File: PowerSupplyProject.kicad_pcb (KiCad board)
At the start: 2 copper layers, 0 parts

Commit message: create pcb design, route and copper fills
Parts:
- added C1: 10u, Capacitor_THT:C_Disc_D3.0mm_W1.6mm_P2.50mm, F.Cu at (126.7, 77.5)
- added C2: 0.1u, Capacitor_THT:C_Disc_D3.0mm_W1.6mm_P2.50mm, F.Cu at (119.4, 77.5)
- added C3: 1u, Capacitor_THT:C_Disc_D3.0mm_W1.6mm_P2.50mm, F.Cu at (120.9, 111.0)
- added D1: LED, LED_THT:LED_D5.0mm, F.Cu at (136.9, 94.5)
- added J1: Conn_01x02_Pin, Connector_PinHeader_2.54mm:PinHeader_1x02_P2.54mm_Vertical, F.Cu at (144.3, 70.1)
- added J2: Conn_01x02_Pin, Connector_PinHeader_2.54mm:PinHeader_1x02_P2.54mm_Vertical, F.Cu at (144.3, 115.9)
- added J3: Conn_01x03_Pin, Connector_PinHeader_2.54mm:PinHeader_1x03_P2.54mm_Vertical, F.Cu at (125.2, 71.1)
- added J4: Conn_01x03_Pin, Connector_PinHeader_2.54mm:PinHeader_1x03_P2.54mm_Vertical, F.Cu at (126.0, 117.6)
- added J5: Screw_Terminal_01x02, TerminalBlockUpdate:TerminalBlock_bornier-2_P5.08mm, F.Cu at (133.0, 72.3)
- added J7: Screw_Terminal_01x02, TerminalBlockUpdate:TerminalBlock_bornier-2_P5.08mm, F.Cu at (133.0, 116.2)
- added J8: Barrel_Jack_Switch, Connector_BarrelJack:BarrelJack_Horizontal, F.Cu at (130.7, 93.2)
- added R1: 330, Resistor_THT:R_Axial_DIN0204_L3.6mm_D1.6mm_P7.62mm_Horizontal, F.Cu at (133.1, 101.9)
- added R2: 330, Resistor_THT:R_Axial_DIN0204_L3.6mm_D1.6mm_P7.62mm_Horizontal, F.Cu at (127.5, 113.8)
- added R3: 560, Resistor_THT:R_Axial_DIN0204_L3.6mm_D1.6mm_P7.62mm_Horizontal, F.Cu at (130.6, 109.5)
- added SW1: EG1218, EG1218:EG1218, F.Cu at (132.2, 79.8)
- added U1: LM7805_TO220, Package_TO_SOT_THT:TO-220-3_Vertical, F.Cu at (124.7, 84.1)
- added U2: LM317_TO-220, Package_TO_SOT_THT:TO-220-3_Vertical, F.Cu at (125.2, 103.1)
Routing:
- net /PWR_output: track 0.00 -> 92.0 mm
- net /3.3V: track 0.00 -> 61.2 mm
- net /5V: track 0.00 -> 49.3 mm
- net /12V: track 0.00 -> 49.0 mm
- net Net-(D1-A): track 0.00 -> 28.3 mm
- net /3V: track 0.00 -> 19.1 mm
- net /PWR_input: track 0.00 -> 14.1 mm
- net Net-(U2-ADJ): track 0.00 -> 8.40 mm
- net Net-(U1-VO): track 0.00 -> 6.69 mm
- added copper zone on B.Cu, net GND
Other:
- board outline added: 30.2 x 52.3 mm

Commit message: fix route
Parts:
- R1: value 330 -> 330R
- R3: value 560 -> 560R
- U1: value LM7805_TO220 -> LM7805
- U2: value LM317_TO-220 -> LM317
- moved R2 22.9 mm to (134.9, 92.1), turned to 90 degrees
- moved D1 3.52 mm to (136.0, 97.9)
- moved U1 3.11 mm to (122.0, 85.6), turned to 0 degrees
- moved R1 2.02 mm to (134.9, 102.8)
- moved U2 1.88 mm to (127.1, 103.1)
- moved R3 1.44 mm to (131.5, 110.5)
- moved C3 1.12 mm to (120.9, 109.9)
- moved J4 0.76 mm to (125.2, 117.6)
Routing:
- net Net-(D1-A): track 28.3 -> 3.69 mm
- net /12V: track 49.0 -> 60.0 mm
- net Net-(U1-VO): track 6.69 -> 13.6 mm
- net /3.3V: track 61.2 -> 63.1 mm
- net /3V: track 19.1 -> 20.4 mm
- net /PWR_output: track 92.0 -> 93.1 mm
- net Net-(U2-ADJ): track 8.40 -> 9.17 mm

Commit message: adding silkscreen
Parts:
- R2: value 330 -> 330R
- moved C3 1.16 mm to (120.6, 111.0)
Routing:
- net /3V: track 20.4 -> 21.6 mm
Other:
- board text added: "+"
- board text added: "-"
- board text added: "3.3V"
- board text added: "5V"
- board text added: "GND"
- board text added: "OFF"
- board text added: "ON"
- board text added: "V1.0 Power Supply"
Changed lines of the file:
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@@
 			(at -7.8796 -3.6576 0)
 			(layer "F.Fab")
+			(hide yes)
 			(effects
 				(font
@@
 		(tags "EG1218 ")
 		(property "Reference" "SW1"
-			(at -2.9972 5.1524 0)
+			(at 2.794 6.016 0)
 			(unlocked yes)
 			(layer "F.SilkS")
@@
 			(unlocked yes)
 			(layer "F.Fab")
+			(hide yes)
 			(effects
 				(font
@@
 		)
 		(fp_text user "*"
-			(at -2.5019 0 90)
-			(layer "F.SilkS")
+			(at -1.4224 -0.0292 90)
+			(unlocked yes)
+			(layer "F.Fab")
 			(effects
 				(font
@@
 		)
 		(fp_text user "*"
-			(at -2.5019 0 90)
-			(unlocked yes)
-			(layer "F.SilkS")
+			(at -1.6129 0 90)
+			(layer "F.Fab")
 			(effects
 				(font
@@
 		)
 		(fp_text user "*"
-			(at -1.6129 0 90)
-			(unlocked yes)
+			(at -1.4732 2.3584 90)
 			(layer "F.Fab")
 			(effects
@@
 		)
 		(fp_text user "*"
-			(at -1.6129 0 90)
+			(at -1.4224 5.8636 90)
+			(unlocked yes)
 			(layer "F.Fab")
 			(effects
@@
 		)
 		(fp_text user "${REFERENCE}"
-			(at -1.524 2.714 0)
+			(at 0.3048 6.524 0)
 			(unlocked yes)
 			(layer "F.Fab")
@@
 			(at 2.54 5.08 0)
 			(layer "F.Fab")
+			(hide yes)
 			(effects
 				(font
@@
 		(tags "Through hole pin header THT 1x02 2.54mm single row")
 		(property "Reference" "J1"
-			(at -2.5908 1.27 90)
+			(at -2.6924 3.5052 90)
 			(layer "F.SilkS")
 			(effects
@@
 			(at 0 4.92 0)
 			(layer "B.Fab")
+			(hide yes)
 			(effects
 				(font
@@
 		(tags "terminal block bornier2")
 		(property "Reference" "J5"
-			(at -3.6931 2.088 90)
+			(at -3.4391 3.5104 90)
 			(layer "F.SilkS")
 			(effects
@@
 			(at 2.54 5.08 0)
 			(layer "F.Fab")
+			(hide yes)
 			(effects
 				(font
@@
 		(tags "TO-220-3 Vertical RM 2.54mm")
 		(property "Reference" "U2"
-			(at 0.5588 -4.1656 0)
+			(at 0 -4.3688 0)
 			(layer "F.SilkS")
 			(effects
@@
 		)
 		(property "Value" "LM317"
-			(at 2.54 2.2 0)
+			(at 3.6576 -4.3688 0)
 			(layer "F.SilkS")
 			(effects
@@
 	(footprint "Capacitor_THT:C_Disc_D3.0mm_W1.6mm_P2.50mm"
 		(layer "F.Cu")
-		(at 120.8932 109.8804)
+		(at 120.5684 110.998)
 		(descr "C, Disc series, Radial, pin pitch=2.50mm, diameter*width=3.0*1.6mm^2, Capacitor, http://www.vishay.com/docs/45233/krseries.pdf")
 		(tags "C Disc series Radial pin pitch 2.50mm diameter 3.0mm width 1.6mm Capacitor")
@@
 			)
 		)
-		(property "Value" "330"
+		(property "Value" "330R"
 			(at 6.4516 1.8288 90)
 			(layer "F.SilkS")
@@
 		(tags "Through hole pin header THT 1x03 2.54mm single row")
 		(property "Reference" "J3"
-			(at 2.54 -0.8128 180)
+			(at -1.1176 -2.54 0)
 			(layer "F.SilkS")
 			(effects
@@
 			(at 0 7.46 90)
 			(layer "F.Fab")
+			(hide yes)
 			(effects
 				(font
@@
 		(tags "Through hole pin header THT 1x03 2.54mm single row")
 		(property "Reference" "J4"
-			(at -2.6924 -0.6604 180)
+			(at 1.1176 -2.794 180)
 			(layer "F.SilkS")
 			(effects
@@
 			(at 0 7.46 90)
 			(layer "F.Fab")
+			(hide yes)
 			(effects
 				(font
@@
 		(tags "Through hole pin header THT 1x02 2.54mm single row")
 		(property "Reference" "J2"
-			(at -2.8448 0.1524 90)
+			(at -2.6924 2.5908 90)
 			(layer "F.SilkS")
 			(effects
@@
 			(at 0 4.92 0)
 			(layer "F.Fab")
+			(hide yes)
 			(effects
 				(font
@@
 		(layer "Edge.Cuts")
 	)
+	(gr_text "5V"
+		(at 118.9736 115.7732 0)
+		(layer "F.SilkS")
+		(effects
+			(font
+				(size 1 1)
+				(thickness 0.2)
+				(bold yes)
+			)
+			(justify left bottom)
+		)
+	)
+	(gr_text "5V"
+		(at 119.0244 74.168 0)
+		(layer "F.SilkS")
+		(effects
+			(font
+				(size 1 1)
+				(thickness 0.2)
+				(bold yes)
+			)
+			(justify left bottom)
+		)
+	)
+	(gr_text "3.3V"
+		(at 123.952 74.2188 0)
+		(layer "F.SilkS")
+		(effects
+			(font
+				(size 1 1)
+				(thickness 0.2)
+				(bold yes)
+			)
+			(justify left bottom)
+		)
+	)
+	(gr_text "3.3V"
+		(at 124.1044 115.7732 0)
+		(layer "F.SilkS")
+		(effects
+			(font
+				(size 1 1)
+				(thickness 0.2)
+				(bold yes)
+			)
+			(justify left bottom)
+		)
+	)
+	(gr_text "ON"
+		(at 131.0132 83.5152 0)
+		(layer "F.SilkS")
+		(effects
+			(font
+				(size 1 1)
+				(thickness 0.2)
+				(bold yes)
+			)
+			(justify left bottom)
+		)
+	)
+	(gr_text "OFF"
+		(at 135.9916 83.566 0)
+		(layer "F.SilkS")
+		(effects
+			(font
+				(size 1 1)
+				(thickness 0.2)
+				(bold yes)
+			)
+			(justify left bottom)
+		)
+	)
+	(gr_text "-"
+		(at 136.8552 98.1964 0)
+		(layer "F.SilkS")
+		(effects
+			(font
+				(size 1 1)
+				(thickness 0.2)
+				(bold yes)
+			)
+			(justify left bottom)
+		)
+	)
+	(gr_text "+"
+		(at 136.9568 96.1644 0)
+		(layer "F.SilkS")
+		(effects
+			(font
+				(size 1 1)
+				(thickness 0.2)
+				(bold yes)
+			)
+			(justify left bottom)
+		)
+	)
+	(gr_text "GND"
+		(at 130.048 118.0592 90)
+		(layer "F.SilkS")
+		(effects
+			(font
+				(size 1 1)
+				(thickness 0.2)
+				(bold yes)
+			)
+			(justify left bottom)
+		)
+	)
+	(gr_text "GND"
+		(at 130.0988 73.9648 90)
+		(layer "F.SilkS")
+		(effects
+			(font
+				(size 1 1)
+				(thickness 0.2)
+				(bold yes)
+			)
+			(justify left bottom)
+		)
+	)
+	(gr_text "GND"
+		(at 142.1892 71.8312 90)
+		(layer "F.SilkS")
+		(effects
+			(font
+				(size 1 1)
+				(thickness 0.2)
+				(bold yes)
+			)
+			(justify left bottom)
+		)
+	)
+	(gr_text "GND"
+		(at 142.1892 117.0432 90)
+		(layer "F.SilkS")
+		(effects
+			(font
+				(size 1 1)
+				(thickness 0.2)
+				(bold yes)
+			)
+			(justify left bottom)
+		)
+	)
+	(gr_text "V1.0\nPower\nSupply"
+		(at 122.0724 92.3544 90)
+		(layer "B.SilkS")
+		(effects
+			(font
+				(size 1 1)
+				(thickness 0.1)
+			)
+			(justify left bottom mirror)
+		)
+	)
 	(segment
 		(start 132.16 79.756)
@@
 	)
 	(segment
-		(start 120.8932 106.7924)
-		(end 124.5616 103.124)
+		(start 124.5616 103.124)
+		(end 120.5684 107.1172)
 		(width 0.25)
 		(layer "F.Cu")
@@
 	)
 	(segment
-		(start 120.8932 109.8804)
-		(end 120.8932 106.7924)
+		(start 120.5684 107.1172)
+		(end 120.5684 110.998)
 		(width 0.25)
 		(layer "F.Cu")

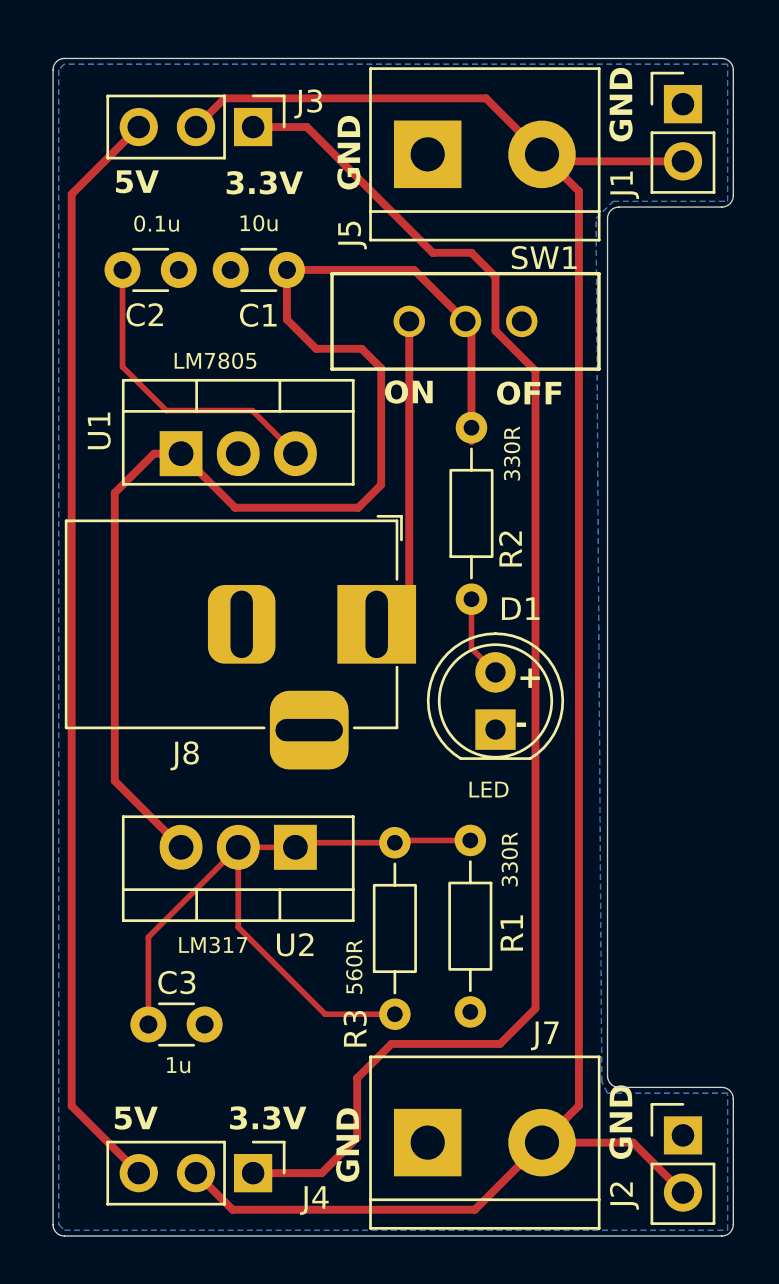
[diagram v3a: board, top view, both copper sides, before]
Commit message: resetting the grid for DfM purposes
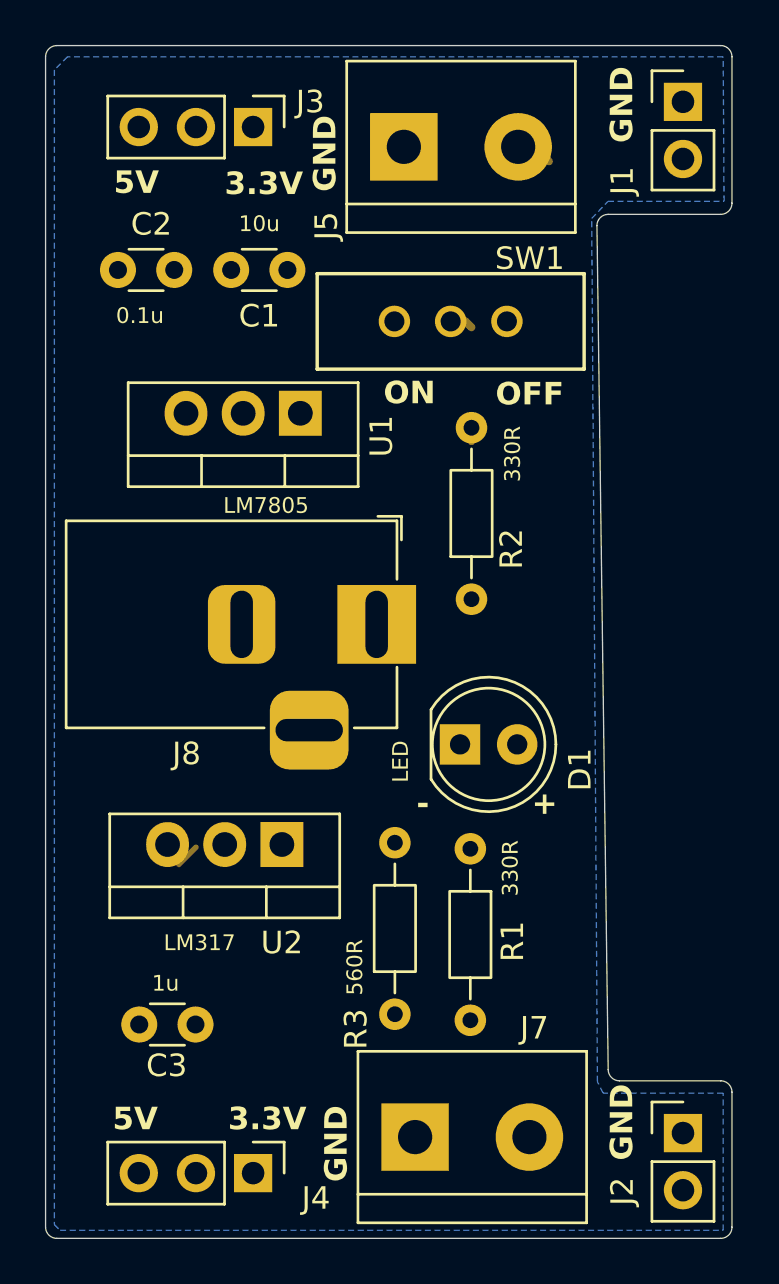
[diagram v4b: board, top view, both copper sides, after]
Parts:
- moved U1 5.59 mm to (127.3, 83.8), turned to 180 degrees
- moved C2 2.30 mm to (121.7, 77.5), turned to 180 degrees
- moved C3 2.09 mm to (122.7, 111.0), turned to 180 degrees
- moved D1 1.71 mm to (134.4, 98.6), turned to 0 degrees
- moved J5 1.11 mm to (131.9, 72.0)
- moved SW1 0.66 mm to (131.5, 79.8)
- moved U2 0.61 mm to (126.5, 103.0)
- moved J7 0.61 mm to (132.4, 116.0)
- moved R1 0.37 mm to (134.9, 103.2)
- moved J1 0.10 mm to (144.3, 70.0)
- moved J2 0.10 mm to (144.3, 115.8)
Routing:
- net /PWR_output: track 93.1 -> 0.44 mm
- net /3.3V: track 63.1 -> 0.00 mm
- net /12V: track 60.0 -> 2.99 mm
- net /5V: track 49.0 -> 0.00 mm
- net /3V: track 21.6 -> 0.00 mm
- net Net-(U1-VO): track 13.6 -> 0.00 mm
- net /PWR_input: track 14.1 -> 2.04 mm
- net Net-(U2-ADJ): track 9.17 -> 0.43 mm
- net Net-(D1-A): track 3.69 -> 0.00 mm
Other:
- board size 30.2 x 52.3 mm -> 30.5 x 53 mm

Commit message: Align all component
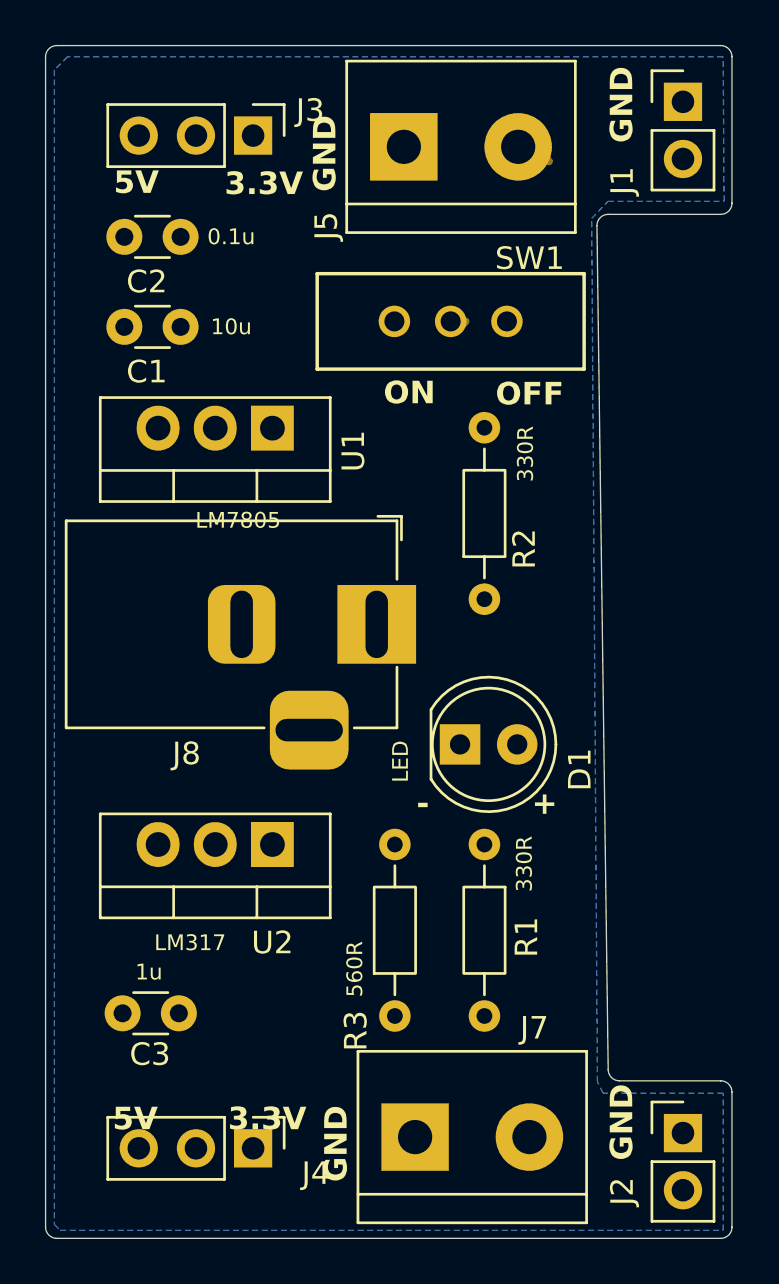
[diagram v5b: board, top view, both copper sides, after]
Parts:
- moved C1 5.38 mm to (122.0, 80.0)
- moved C2 1.50 mm to (122.0, 76.0)
- moved U1 1.40 mm to (126.1, 84.5)
- moved J4 1.10 mm to (125.2, 116.5)
- moved C3 0.89 mm to (121.9, 110.5)
- moved R1 0.65 mm to (135.5, 103.0)
- moved R2 0.58 mm to (135.5, 92.1)
- moved U2 0.42 mm to (126.1, 103.0)
- moved J3 0.38 mm to (125.2, 71.5)
- moved R3 0.08 mm to (131.5, 110.6)
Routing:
- net /12V: track 2.99 -> 0.36 mm
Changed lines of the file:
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@@
 		(capping no)
 		(filling no)
-		(zone_defaults)
 		(pcbplotparams
 			(layerselection 0x00000000_00000000_55555555_5755f5ff)
@@
 	(footprint "Resistor_THT:R_Axial_DIN0204_L3.6mm_D1.6mm_P7.62mm_Horizontal"
 		(layer "F.Cu")
-		(at 131.5212 110.5408 90)
+		(at 131.5212 110.62 90)
 		(descr "Resistor, Axial_DIN0204 series, Axial, Horizontal, pin pitch=7.62mm, 0.167W, length*diameter=3.6*1.6mm^2, http://cdn-reichelt.de/documents/datenblatt/B400/1_4W%23YAG.pdf")
 		(tags "Resistor Axial_DIN0204 series Axial Horizontal pin pitch 7.62mm 0.167W length 3.6mm diameter 1.6mm")
@@
 	(footprint "Package_TO_SOT_THT:TO-220-3_Vertical"
 		(layer "F.Cu")
-		(at 126.5 103 180)
+		(at 126.08 103 180)
 		(descr "TO-220-3, Vertical, RM 2.54mm, see https://www.vishay.com/docs/66542/to-220-1.pdf")
 		(tags "TO-220-3 Vertical RM 2.54mm")
@@
 	(footprint "Capacitor_THT:C_Disc_D3.0mm_W1.6mm_P2.50mm"
 		(layer "F.Cu")
-		(at 122.662 110.998 180)
+		(at 121.922 110.5 180)
 		(descr "C, Disc series, Radial, pin pitch=2.50mm, diameter*width=3.0*1.6mm^2, Capacitor, http://www.vishay.com/docs/45233/krseries.pdf")
 		(tags "C Disc series Radial pin pitch 2.50mm diameter 3.0mm width 1.6mm Capacitor")
@@
 	(footprint "Capacitor_THT:C_Disc_D3.0mm_W1.6mm_P2.50mm"
 		(layer "F.Cu")
-		(at 126.746 77.47 180)
+		(at 122 80 180)
 		(descr "C, Disc series, Radial, pin pitch=2.50mm, diameter*width=3.0*1.6mm^2, Capacitor, http://www.vishay.com/docs/45233/krseries.pdf")
 		(tags "C Disc series Radial pin pitch 2.50mm diameter 3.0mm width 1.6mm Capacitor")
 		(property "Reference" "C1"
-			(at 1.25 -2.05 0)
+			(at 1.5 -2 0)
 			(layer "F.SilkS")
 			(effects
@@
 		)
 		(property "Value" "10u"
-			(at 1.25 2.05 0)
+			(at -2.25 0 0)
 			(layer "F.SilkS")
 			(effects
@@
 	(footprint "Resistor_THT:R_Axial_DIN0204_L3.6mm_D1.6mm_P7.62mm_Horizontal"
 		(layer "F.Cu")
-		(at 134.9248 92.1004 90)
+		(at 135.5 92.1004 90)
 		(descr "Resistor, Axial_DIN0204 series, Axial, Horizontal, pin pitch=7.62mm, 0.167W, length*diameter=3.6*1.6mm^2, http://cdn-reichelt.de/documents/datenblatt/B400/1_4W%23YAG.pdf")
 		(tags "Resistor Axial_DIN0204 series Axial Horizontal pin pitch 7.62mm 0.167W length 3.6mm diameter 1.6mm")
@@
 	(footprint "Connector_PinHeader_2.54mm:PinHeader_1x03_P2.54mm_Vertical"
 		(layer "F.Cu")
-		(at 125.222 71.12 -90)
+		(at 125.222 71.5 -90)
 		(descr "Through hole straight pin header, 1x03, 2.54mm pitch, single row")
 		(tags "Through hole pin header THT 1x03 2.54mm single row")
@@
 	(footprint "Connector_PinHeader_2.54mm:PinHeader_1x03_P2.54mm_Vertical"
 		(layer "F.Cu")
-		(at 125.222 117.602 -90)
+		(at 125.222 116.5 -90)
 		(descr "Through hole straight pin header, 1x03, 2.54mm pitch, single row")
 		(tags "Through hole pin header THT 1x03 2.54mm single row")
@@
 	(footprint "Resistor_THT:R_Axial_DIN0204_L3.6mm_D1.6mm_P7.62mm_Horizontal"
 		(layer "F.Cu")
-		(at 134.874 103.19 -90)
+		(at 135.5 103 -90)
 		(descr "Resistor, Axial_DIN0204 series, Axial, Horizontal, pin pitch=7.62mm, 0.167W, length*diameter=3.6*1.6mm^2, http://cdn-reichelt.de/documents/datenblatt/B400/1_4W%23YAG.pdf")
 		(tags "Resistor Axial_DIN0204 series Axial Horizontal pin pitch 7.62mm 0.167W length 3.6mm diameter 1.6mm")
@@
 	(footprint "Package_TO_SOT_THT:TO-220-3_Vertical"
 		(layer "F.Cu")
-		(at 127.32 83.84 180)
+		(at 126.08 84.5 180)
 		(descr "TO-220-3, Vertical, RM 2.54mm, see https://www.vishay.com/docs/66542/to-220-1.pdf")
 		(tags "TO-220-3 Vertical RM 2.54mm")
@@
 	(footprint "Capacitor_THT:C_Disc_D3.0mm_W1.6mm_P2.50mm"
 		(layer "F.Cu")
-		(at 121.7168 77.47 180)
+		(at 122 76 180)
 		(descr "C, Disc series, Radial, pin pitch=2.50mm, diameter*width=3.0*1.6mm^2, Capacitor, http://www.vishay.com/docs/45233/krseries.pdf")
 		(tags "C Disc series Radial pin pitch 2.50mm diameter 3.0mm width 1.6mm Capacitor")
 		(property "Reference" "C2"
-			(at 1.016 2.032 0)
+			(at 1.5 -2 0)
 			(layer "F.SilkS")
 			(effects
@@
 		)
 		(property "Value" "0.1u"
-			(at 1.524 -2.032 0)
+			(at -2.25 0 0)
 			(layer "F.SilkS")
 			(effects
@@
 	)
 	(segment
-		(start 127.3048 102.9208)
-		(end 127.1016 103.124)
-		(width 0.25)
-		(layer "F.Cu")
-		(net "Net-(U2-ADJ)")
-	)
-	(segment
 		(start 131.6228 102.8192)
 		(end 131.5212 102.9208)
@@
 		(layer "F.Cu")
 		(net "/12V")
-	)
-	(segment
-		(start 134.9248 84.4804)
-		(end 134.9248 85.0798)
-		(width 0.35)
-		(layer "F.Cu")
-		(net "/12V")
-	)
-	(segment
-		(start 126.726 77.47)
-		(end 126.726 77.8056)
-		(width 0.35)
-		(layer "F.Cu")
-		(net "/12V")
-	)
-	(segment
-		(start 126.726 77.8056)
-		(end 126.8984 77.978)
-		(width 0.35)
-		(layer "F.Cu")
-		(net "/12V")
-	)
-	(segment
-		(start 134.9248 80.0208)
-		(end 134.66 79.756)
-		(width 0.35)
-		(layer "F.Cu")
-		(net "/12V")
-	)
-	(segment
-		(start 122.682 103.124)
-		(end 121.92 103.886)
-		(width 0.25)
-		(layer "F.Cu")
-		(net "/12V")
